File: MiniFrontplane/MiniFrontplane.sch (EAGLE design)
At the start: 13 parts, among them IC2 74ACT14N, U1 MCP130SOT

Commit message: Frontplane THAT MIGHT WORK THIS TIME
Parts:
- removed C1: 4.7uF, SparkFun-Passives:CAPEZ
- removed IC2: 74ACT14N, 74xx-eu:74ACT14N
- removed R2: 4k7, SparkFun-Resistors:RESISTORAXIAL-0.3
- removed R3, R4: 27k, SparkFun-Resistors:RESISTORAXIAL-0.3
- removed U$1: MINITOGGLE, Benchoff:MINITOGGLE
- removed U$2: MINITACT, Benchoff:MINITACT
- added S1: TP11SWITCH, Benchoff:TP11SWITCH
- added S2: MINITOGGLE, Benchoff:MINITOGGLE
- JP3: value Samtec SLW-103-01-T-S -> (none)
- LED1: device SparkFun-LED:LED5MM -> led:LED5MM
- R1: value 150 -> 220; device SparkFun-Resistors:RESISTORAXIAL-0.3 -> SparkFun-Resistors:RESISTORKIT
- U1: value MCP130SOT -> DS1813; device SparkFun-DigitalIC:MCP130SOT -> Benchoff:DS1813
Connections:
- net N$2 renamed PS_OK
- removed net 5VSB: JP1.3
- removed net N$1 (its old number): JP3.1, U$1.P3
- removed net N$4: R3.2, R4.1, U$2.CON2
- removed net N$5: C1.2, R2.2, R3.1
- removed net N$6: IC2A.I, R2.1
- new net PS_ON: JP3.3, S2.L2
- net GND: now also JP2.31, JP3.1, S1.P$2, S2.COM; no longer JP2.2, JP3.3, R4.2, U$1.COM
- net RESET: now also JP1.27, S1.P$1, U1./RST; no longer IC2A.O, JP2.28, U1.RESET
- net VCC: no longer C1.1, U$2.CON1
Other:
- moved on the sheet: LED1, R1

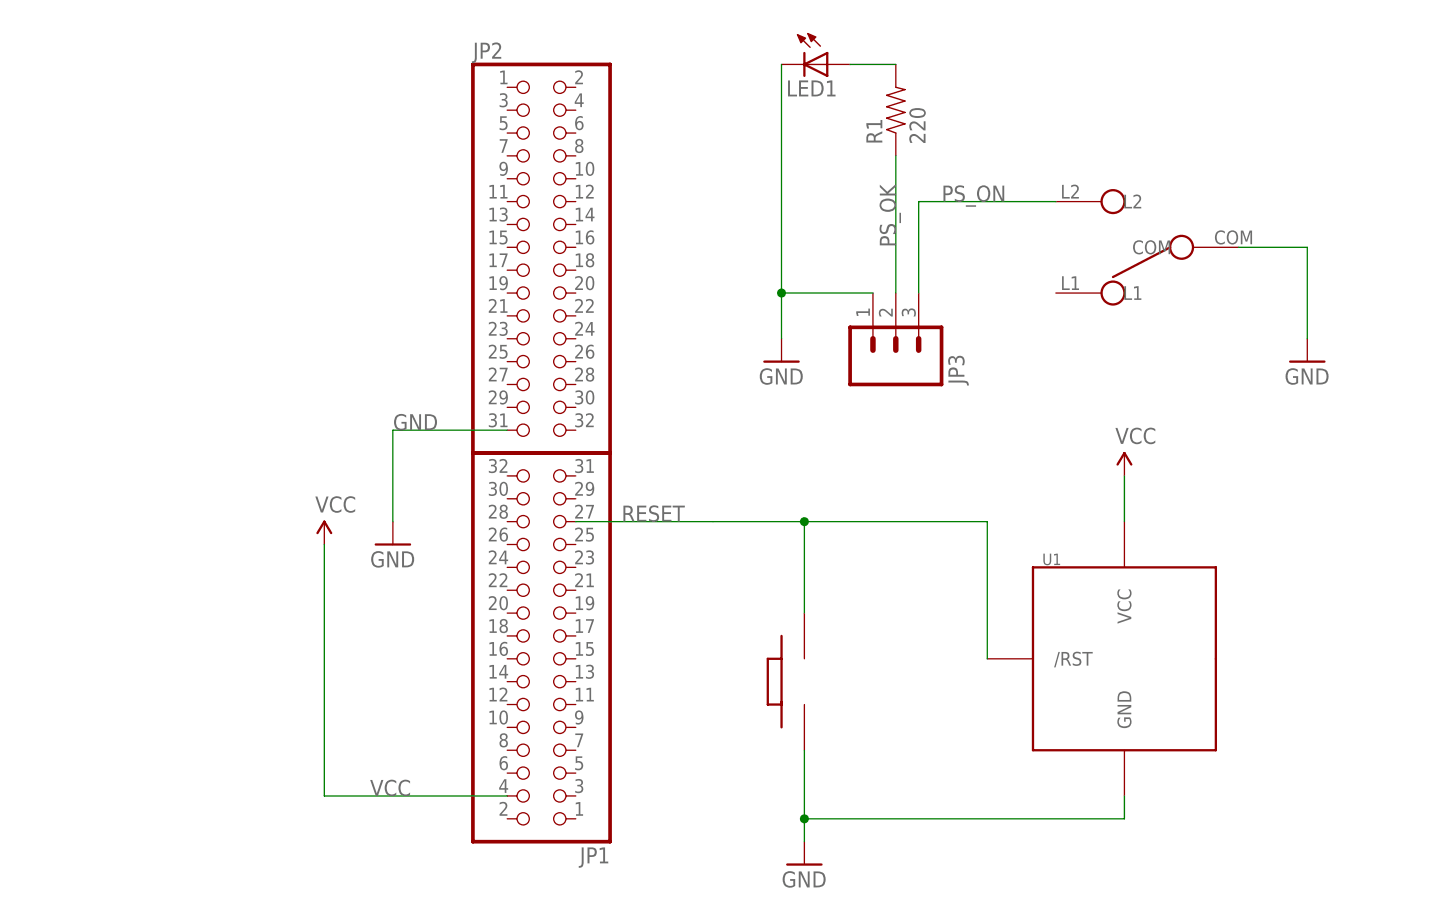
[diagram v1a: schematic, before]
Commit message: Fixed the mini front plane
It didn't work before, so there ya go
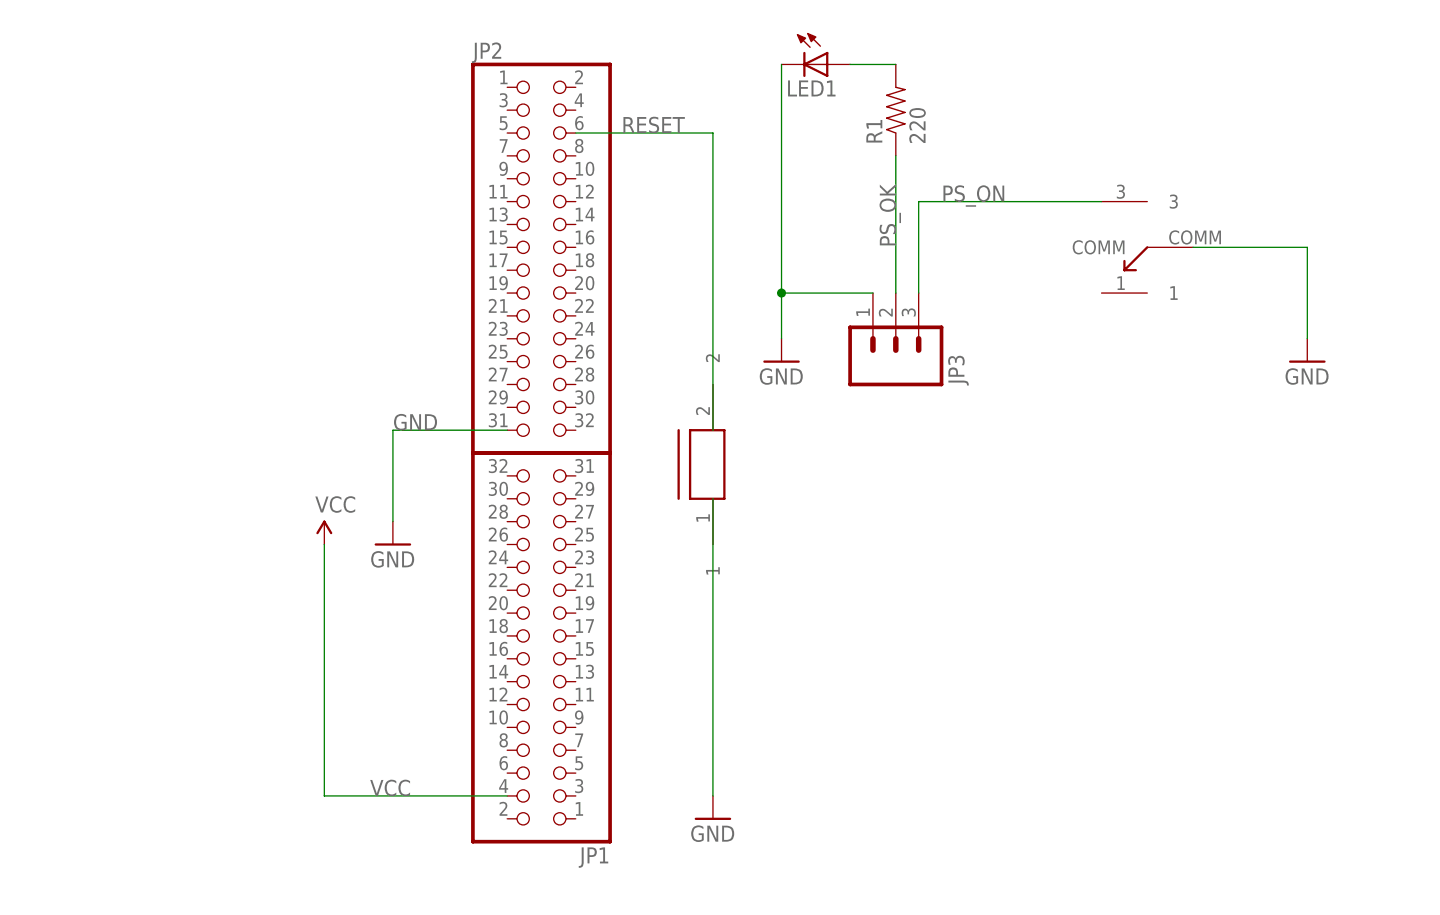
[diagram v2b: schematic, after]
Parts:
- removed S1: TP11SWITCH, Benchoff:TP11SWITCH
- removed S2: MINITOGGLE, Benchoff:MINITOGGLE
- removed U1: DS1813, Benchoff:DS1813
- added U$1: 7101, C&K:7101
- added U$2: TP11, C&K:TP11
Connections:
- net GND: now also U$1.COMM, U$2.1; no longer S1.P$2, S2.COM, U1.GND
- net PS_ON: now also U$1.3; no longer S2.L2
- net RESET: now also JP2.6, U$2.2; no longer JP1.27, S1.P$1, U1./RST
- net VCC: no longer U1.VCC
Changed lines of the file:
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@@
 <?xml version="1.0" encoding="utf-8"?>
 <!DOCTYPE eagle SYSTEM "eagle.dtd">
-<eagle version="6.4">
+<eagle version="6.6.0">
 <drawing>
 <settings>
@@
 <part name="GND2" library="SparkFun-Aesthetics" deviceset="GND" device=""/>
 <part name="SUPPLY4" library="SparkFun-Aesthetics" deviceset="VCC" device=""/>
-<part name="S1" library="Benchoff" deviceset="TP11SWITCH" device=""/>
-<part name="S2" library="Benchoff" deviceset="MINITOGGLE" device=""/>
 <part name="GND3" library="SparkFun-Aesthetics" deviceset="GND" device=""/>
 <part name="LED1" library="led" deviceset="LED" device="5MM"/>
 <part name="R1" library="SparkFun-Resistors" deviceset="RESISTOR" device="KIT" value="220"/>
 <part name="GND4" library="SparkFun-Aesthetics" deviceset="GND" device=""/>
-<part name="U1" library="Benchoff" deviceset="DS1813" device=""/>
-<part name="SUPPLY1" library="SparkFun-Aesthetics" deviceset="VCC" device=""/>
+<part name="U$1" library="C&amp;K" deviceset="7101" device=""/>
+<part name="U$2" library="C&amp;K" deviceset="TP11" device=""/>
 </parts>
 <sheets>
@@
 <instance part="JP3" gate="G$1" x="63.5" y="60.96" rot="MR90"/>
 <instance part="GND1" gate="1" x="50.8" y="60.96"/>
-<instance part="GND2" gate="1" x="53.34" y="5.08"/>
+<instance part="GND2" gate="1" x="43.18" y="10.16"/>
 <instance part="SUPPLY4" gate="1" x="0" y="40.64"/>
-<instance part="S1" gate="G$1" x="53.34" y="25.4"/>
-<instance part="S2" gate="G$1" x="91.44" y="73.66" rot="R180"/>
 <instance part="GND3" gate="1" x="7.62" y="40.64"/>
 <instance part="LED1" gate="G$1" x="55.88" y="93.98" rot="R270"/>
 <instance part="R1" gate="G$1" x="63.5" y="88.9" rot="R90"/>
 <instance part="GND4" gate="1" x="109.22" y="60.96"/>
-<instance part="U1" gate="G$1" x="88.9" y="27.94"/>
-<instance part="SUPPLY1" gate="1" x="88.9" y="48.26"/>
+<instance part="U$1" gate="G$1" x="91.44" y="73.66" rot="R180"/>
+<instance part="U$2" gate="G$1" x="43.18" y="50.8" rot="R90"/>
 </instances>
 <busses>
@@
 <net name="RESET" class="0">
 <segment>
-<label x="33.02" y="43.18" size="1.778" layer="95"/>
-<pinref part="JP1" gate="A" pin="27"/>
-<wire x1="27.94" y1="43.18" x2="43.18" y2="43.18" width="0.1524" layer="91"/>
-<wire x1="43.18" y1="43.18" x2="53.34" y2="43.18" width="0.1524" layer="91"/>
-<pinref part="S1" gate="G$1" pin="P$1"/>
-<wire x1="53.34" y1="43.18" x2="53.34" y2="33.02" width="0.1524" layer="91"/>
-<pinref part="U1" gate="G$1" pin="/RST"/>
-<wire x1="53.34" y1="43.18" x2="73.66" y2="43.18" width="0.1524" layer="91"/>
-<wire x1="73.66" y1="43.18" x2="73.66" y2="27.94" width="0.1524" layer="91"/>
-<junction x="53.34" y="43.18"/>
+<label x="33.02" y="86.36" size="1.778" layer="95"/>
+<pinref part="U$2" gate="G$1" pin="2"/>
+<wire x1="43.18" y1="86.36" x2="43.18" y2="53.34" width="0.1524" layer="91"/>
+<pinref part="JP2" gate="A" pin="6"/>
+<wire x1="43.18" y1="86.36" x2="27.94" y2="86.36" width="0.1524" layer="91"/>
 </segment>
 </net>
@@
 <wire x1="0" y1="40.64" x2="0" y2="12.7" width="0.1524" layer="91"/>
 </segment>
-<segment>
-<pinref part="SUPPLY1" gate="1" pin="VCC"/>
-<pinref part="U1" gate="G$1" pin="VCC"/>
-<wire x1="88.9" y1="48.26" x2="88.9" y2="43.18" width="0.1524" layer="91"/>
-</segment>
 </net>
 <net name="GND" class="0">
@@
 </segment>
 <segment>
-<pinref part="S1" gate="G$1" pin="P$2"/>
 <pinref part="GND2" gate="1" pin="GND"/>
-<wire x1="53.34" y1="17.78" x2="53.34" y2="10.16" width="0.1524" layer="91"/>
-<pinref part="U1" gate="G$1" pin="GND"/>
-<wire x1="53.34" y1="10.16" x2="53.34" y2="7.62" width="0.1524" layer="91"/>
-<wire x1="88.9" y1="12.7" x2="88.9" y2="10.16" width="0.1524" layer="91"/>
-<wire x1="88.9" y1="10.16" x2="53.34" y2="10.16" width="0.1524" layer="91"/>
-<junction x="53.34" y="10.16"/>
+<wire x1="43.18" y1="12.7" x2="43.18" y2="45.72" width="0.1524" layer="91"/>
+<pinref part="U$2" gate="G$1" pin="1"/>
 </segment>
 <segment>
@@
 </segment>
 <segment>
-<pinref part="S2" gate="G$1" pin="COM"/>
 <pinref part="GND4" gate="1" pin="GND"/>
-<wire x1="101.6" y1="73.66" x2="109.22" y2="73.66" width="0.1524" layer="91"/>
+<wire x1="96.52" y1="73.66" x2="109.22" y2="73.66" width="0.1524" layer="91"/>
 <wire x1="109.22" y1="73.66" x2="109.22" y2="63.5" width="0.1524" layer="91"/>
+<pinref part="U$1" gate="G$1" pin="COMM"/>
 </segment>
 </net>
@@
 <net name="PS_ON" class="0">
 <segment>
-<pinref part="S2" gate="G$1" pin="L2"/>
 <pinref part="JP3" gate="G$1" pin="3"/>
-<wire x1="81.28" y1="78.74" x2="66.04" y2="78.74" width="0.1524" layer="91"/>
+<wire x1="81.28" y1="78.74" x2="78.74" y2="78.74" width="0.1524" layer="91"/>
+<wire x1="78.74" y1="78.74" x2="66.04" y2="78.74" width="0.1524" layer="91"/>
 <wire x1="66.04" y1="78.74" x2="66.04" y2="68.58" width="0.1524" layer="91"/>
 <label x="68.58" y="78.74" size="1.778" layer="95"/>
-</segment>
-</net>
+<pinref part="U$1" gate="G$1" pin="3"/>
+<wire x1="86.36" y1="78.74" x2="81.28" y2="78.74" width="0.1524" layer="91"/>
+</segment>
+</net>
